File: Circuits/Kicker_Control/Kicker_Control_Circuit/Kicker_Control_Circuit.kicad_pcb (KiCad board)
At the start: 2 copper layers, 3 parts, among them U1 VS-5EWH06FN-M3

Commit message: kicker circuit changest
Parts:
- removed D2: SMAJ20A, SMAJ20A:DIOM4325X250N
- removed U1: VS-5EWH06FN-M3, VS-5EWH06FN-M3:DPAK_06FN-M3_VIS
- added 300VJ4: Conn_01x01_Pin, Connector_PinHeader_2.54mm:PinHeader_1x01_P2.54mm_Vertical, F.Cu at (92.5, 68.0)
- added C1: 0.1u, Capacitor_SMD:C_1812_4532Metric, F.Cu at (104.0, 94.5)
- added C2: 0.1u, Capacitor_SMD:C_1206_3216Metric, F.Cu at (92.0, 94.5)
- added C3: 1u, Capacitor_SMD:C_1206_3216Metric, F.Cu at (87.5, 94.5)
- added IC1: UCC27511DBVR, UCC27511DBVR:SOT95P280X145-6N, F.Cu at (88.8, 88.0)
- added J3: Conn_01x03_Pin, Connector_PinHeader_2.54mm:PinHeader_1x03_P2.54mm_Vertical, F.Cu at (84.0, 87.0)
- added Q2: IKB40N65ES5ATMA1, IKB40N65ES5ATMA1 IGBT:BTS141TCBUMA1, F.Cu at (113.0, 78.4)
- added R1: 10k, Resistor_SMD:R_1210_3225Metric, F.Cu at (97.5, 94.5)
- added R2: 10k, Resistor_SMD:R_1210_3225Metric, F.Cu at (95.5, 86.0)
- added R3: 10k, Resistor_SMD:R_1210_3225Metric, F.Cu at (95.5, 89.5)
- added R4: 100, Resistor_SMD:R_2010_5025Metric, F.Cu at (102.5, 89.5)
- added Solenoid+1: Solenoid-, Connector_PinHeader_2.54mm:PinHeader_1x02_P2.54mm_Vertical, F.Cu at (101.3, 68.0)
- added U2: VS-5EWH06FN-M3, VS-5EWH06FN-M3:DPAK_06FN-M3_VIS, F.Cu at (99.5, 77.5)
- D1: value TLP3910_C20-TP,E -> Diode; footprint TLP3910_C20-TP,E:SOIC127P1000X220-6N -> Diode_SMD:D_SMC
- moved D1 36.5 mm to (111.5, 93.0), turned to 90 degrees
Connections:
- D1 pad 1: /LT3751 Capacitor Charger/On_signal/Off_signal -> /GND
- D1 pad 2: unconnected-(D1-N.C.-Pad2) -> Net-(D1-C)
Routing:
- net /GND: track 0.00 -> 59.8 mm
- net Net-(D1-C): track 0.00 -> 18.1 mm
- net /Output2_Solenoid : track 0.00 -> 17.3 mm
- net /Output1_Solenoid : track 0.00 -> 16.2 mm
- net /15V: track 0.00 -> 13.9 mm
- net Net-(R1-Pad1): track 0.00 -> 10.6 mm
- net Net-(IC1-OUTH): track 0.00 -> 4.60 mm
- net Net-(IC1-OUTL): track 0.00 -> 4.49 mm
- net /On_Signal 3V: track 0.00 -> 3.71 mm
- added copper zone on B.Cu, net /GND
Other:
- board outline added: 38.5 x 33 mm

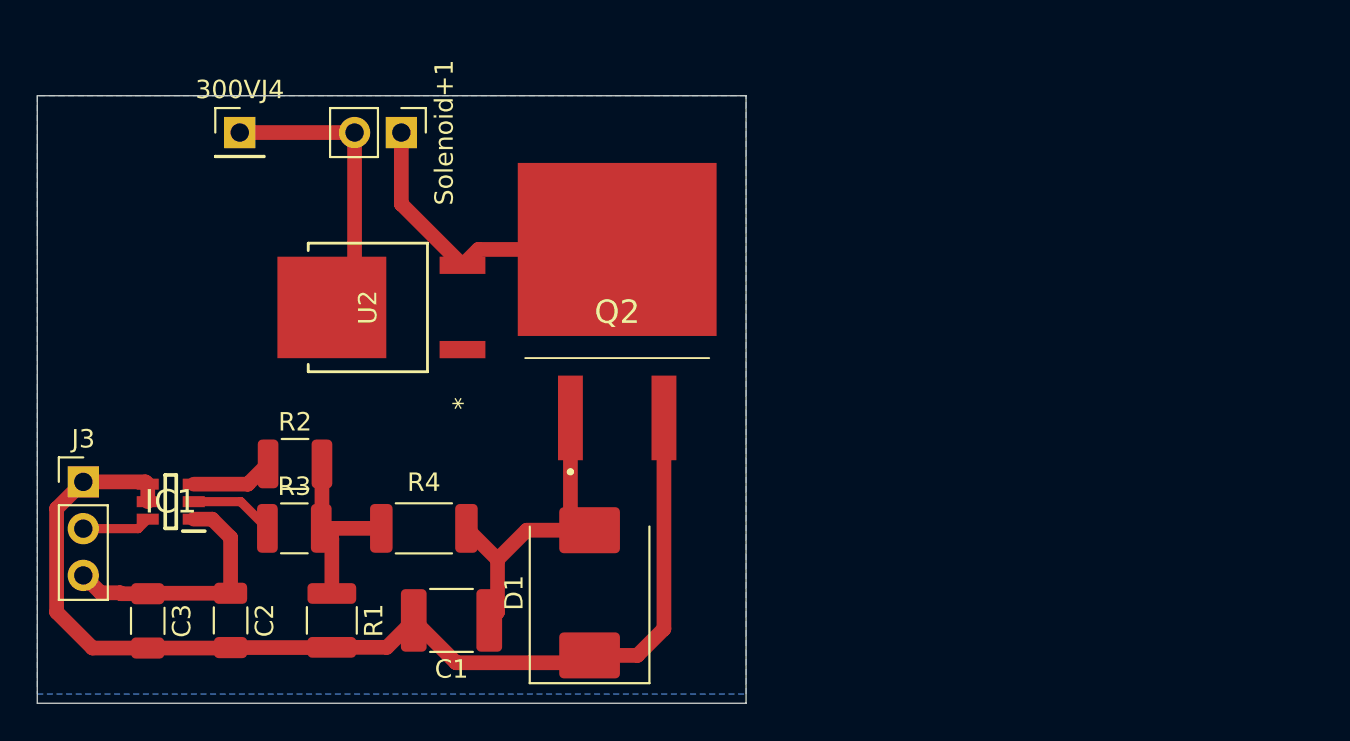
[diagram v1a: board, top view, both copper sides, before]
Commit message: Updated the capacitor footprints to 0805, since everyone was different. Added powerplane and groundplane, vias for ground connections, added a connector to for the solenoid to a 1x2 pin headers since those are easier to find. Changed the connections for the output1_solenoid and outpu2_solenoid to have separate connectors, maybe not necessary
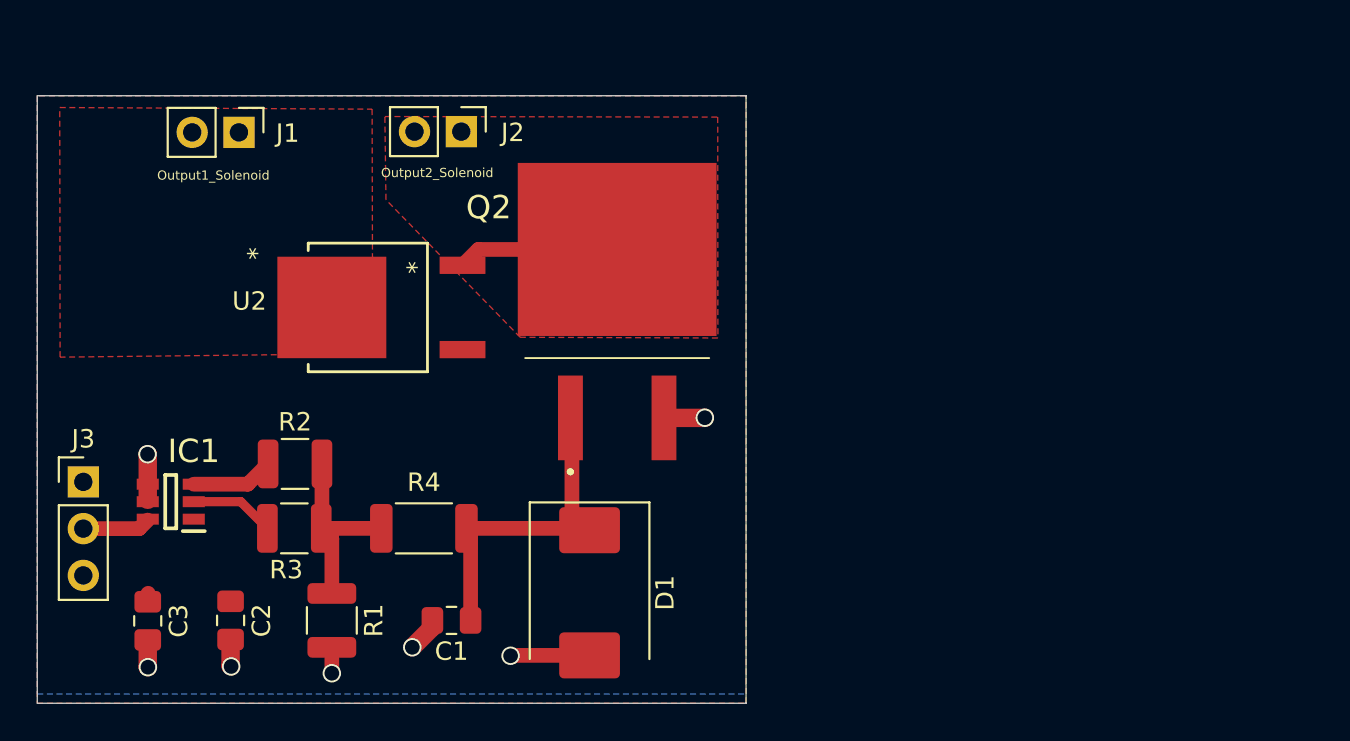
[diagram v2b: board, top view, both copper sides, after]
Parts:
- removed 300VJ4: Conn_01x01_Pin, Connector_PinHeader_2.54mm:PinHeader_1x01_P2.54mm_Vertical
- added J1: Conn_01x02_Pin, Connector_PinHeader_2.54mm:PinHeader_1x02_P2.54mm_Vertical, F.Cu at (92.5, 68.0)
- C1: footprint Capacitor_SMD:C_1812_4532Metric -> Capacitor_SMD:C_0805_2012Metric_Pad1.18x1.45mm_HandSolder
- C2, C3: footprint Capacitor_SMD:C_1206_3216Metric -> Capacitor_SMD:C_0805_2012Metric_Pad1.18x1.45mm_HandSolder
- J2: renamed from Solenoid+1; value Solenoid- -> Conn_01x02_Pin
- moved J2 3.26 mm to (104.5, 68.0)
- turned D1 to -90 degrees
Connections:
- C1 pad 1: Net-(D1-C) -> Net-(D1-K)
- C1 pad 2: /GND -> GND
- C2 pad 2: /GND -> GND
- C3 pad 2: /GND -> GND
- D1 pad 1: /GND -> Net-(D1-K)
- D1 pad 2: Net-(D1-C) -> GND
- IC1 pad 4: /GND -> GND
- IC1 pad 5: /GND -> GND
- J2 pad 2: /Output1_Solenoid  -> /Output2_Solenoid 
- J3 pad 1: /GND -> GND
- Q2 pad 1: Net-(D1-C) -> Net-(D1-K)
- Q2 pad 3: /GND -> GND
- R1 pad 2: /GND -> GND
- R4 pad 2: Net-(D1-C) -> Net-(D1-K)
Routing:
- net /GND: track 59.8 -> 0.00 mm
- net Net-(D1-K): track 0.00 -> 18.4 mm
- net Net-(D1-C): track 18.1 -> 0.00 mm
- net GND: track 0.00 -> 15.9 mm, vias 0 -> 7
- net /Output1_Solenoid : track 16.2 -> 1.75 mm
- net /15V: track 13.9 -> 0.04 mm
- net /Output2_Solenoid : track 17.3 -> 8.76 mm
- added copper zone on F.Cu, net /15V
- added copper zone on F.Cu, net /Output1_Solenoid 
- added copper zone on F.Cu, net /Output2_Solenoid 
- added copper zone on B.Cu, net GND
- removed copper zone on B.Cu, net /GND
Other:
- board text added: "Output1_Solenoid"
- board text added: "Output2_Solenoid"
